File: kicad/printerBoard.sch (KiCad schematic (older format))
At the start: 10 parts

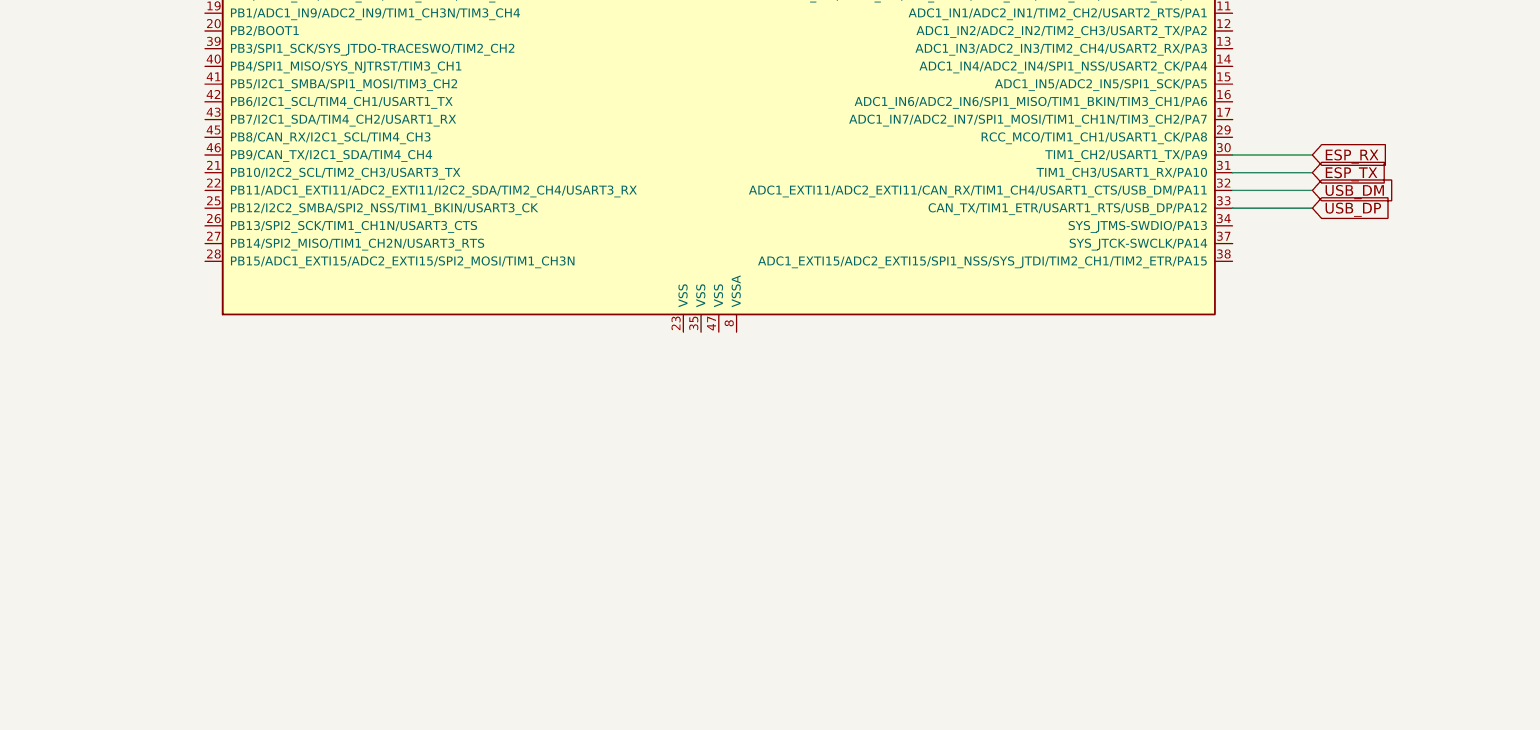
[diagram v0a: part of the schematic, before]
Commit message: Adding A and B motor drivers
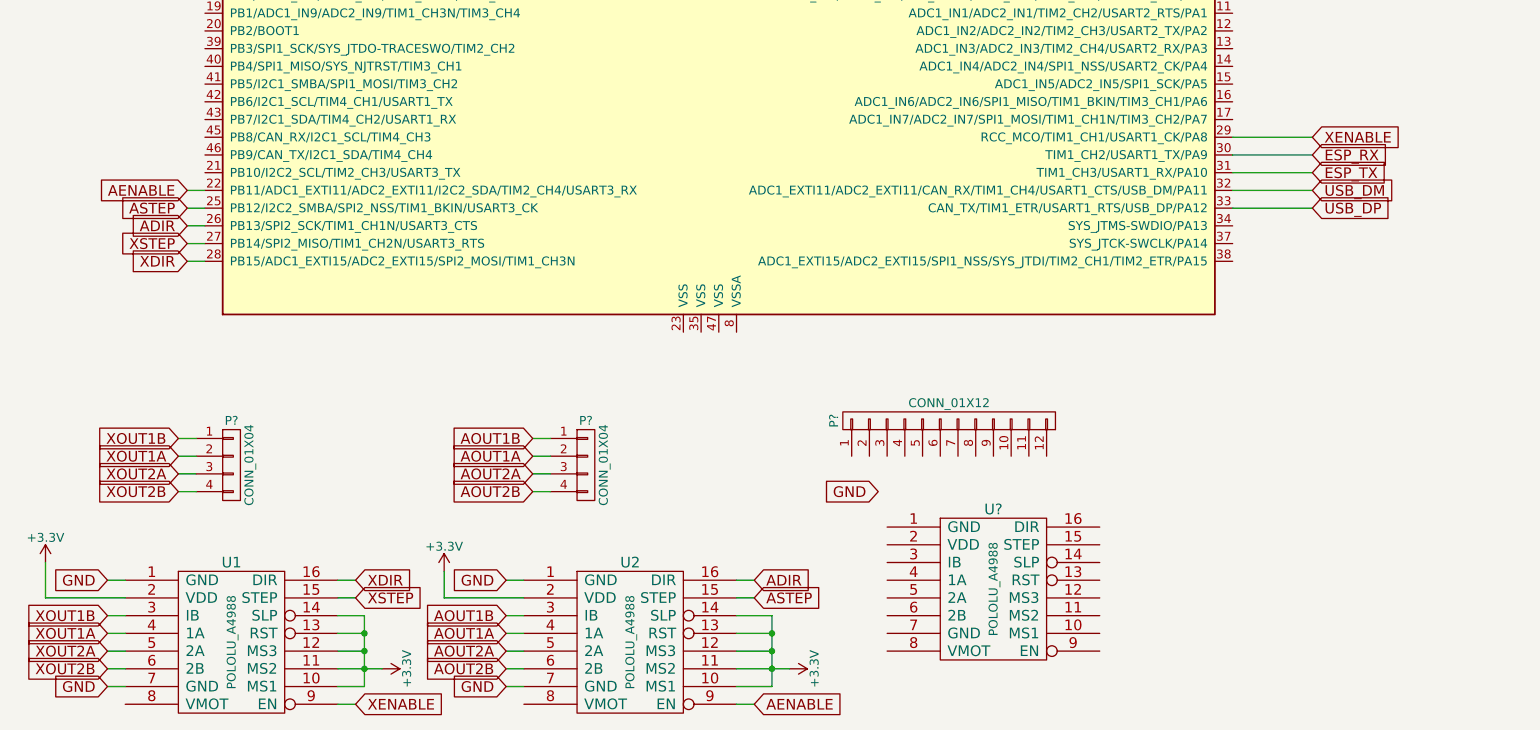
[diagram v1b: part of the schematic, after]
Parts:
- added P? (x2): CONN_01X04, symbol CONN_01X04
- added P?: CONN_01X12, symbol CONN_01X12
- added U1, U2, U?: POLOLU_A4988, symbol POLOLU_A4988
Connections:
- net +3V3: now also U1.10 (MS1), U1.11 (MS2), U1.12 (MS3), U1.13 (RST), U1.14 (SLP), U1.2 (VDD), U2.10 (MS1), U2.11 (MS2), U2.12 (MS3), U2.13 (RST), U2.14 (SLP), U2.2 (VDD)
- net GND: now also U1.1 (GND), U1.7 (GND), U2.1 (GND), U2.7 (GND)
- net AENABLE: now reaches U?.22 (PB11/ADC1_EXTI11/ADC2_EXTI11/I2C2_SDA/TIM2_CH4/USART3_RX)
- net AENABLE: now also U2.9 (EN)
- net ASTEP: now reaches U?.25 (PB12/I2C2_SMBA/SPI2_NSS/TIM1_BKIN/USART3_CK)
- net ASTEP: now also U2.15 (STEP)
- net ADIR: now reaches U?.26 (PB13/SPI2_SCK/TIM1_CH1N/USART3_CTS)
- net ADIR: now also U2.16 (DIR)
- net XSTEP: now reaches U?.27 (PB14/SPI2_MISO/TIM1_CH2N/USART3_RTS)
- net XSTEP: now also U1.15 (STEP)
- net XDIR: now reaches U?.28 (PB15/ADC1_EXTI15/ADC2_EXTI15/SPI2_MOSI/TIM1_CH3N)
- net XDIR: now also U1.16 (DIR)
- net XENABLE: now reaches U?.29 (RCC_MCO/TIM1_CH1/USART1_CK/PA8)
- net XENABLE: now also U1.9 (EN)
- new net AOUT1A: P?.2 (P2), U2.4 (1A)
- new net AOUT1B: P?.1 (P1), U2.3 (IB)
- new net AOUT2A: P?.3 (P3), U2.5 (2A)
- new net AOUT2B: P?.4 (P4), U2.6 (2B)
- new net XOUT1A: P?.2 (P2), U1.4 (1A)
- new net XOUT1B: P?.1 (P1), U1.3 (IB)
- new net XOUT2A: P?.3 (P3), U1.5 (2A)
- new net XOUT2B: P?.4 (P4), U1.6 (2B)

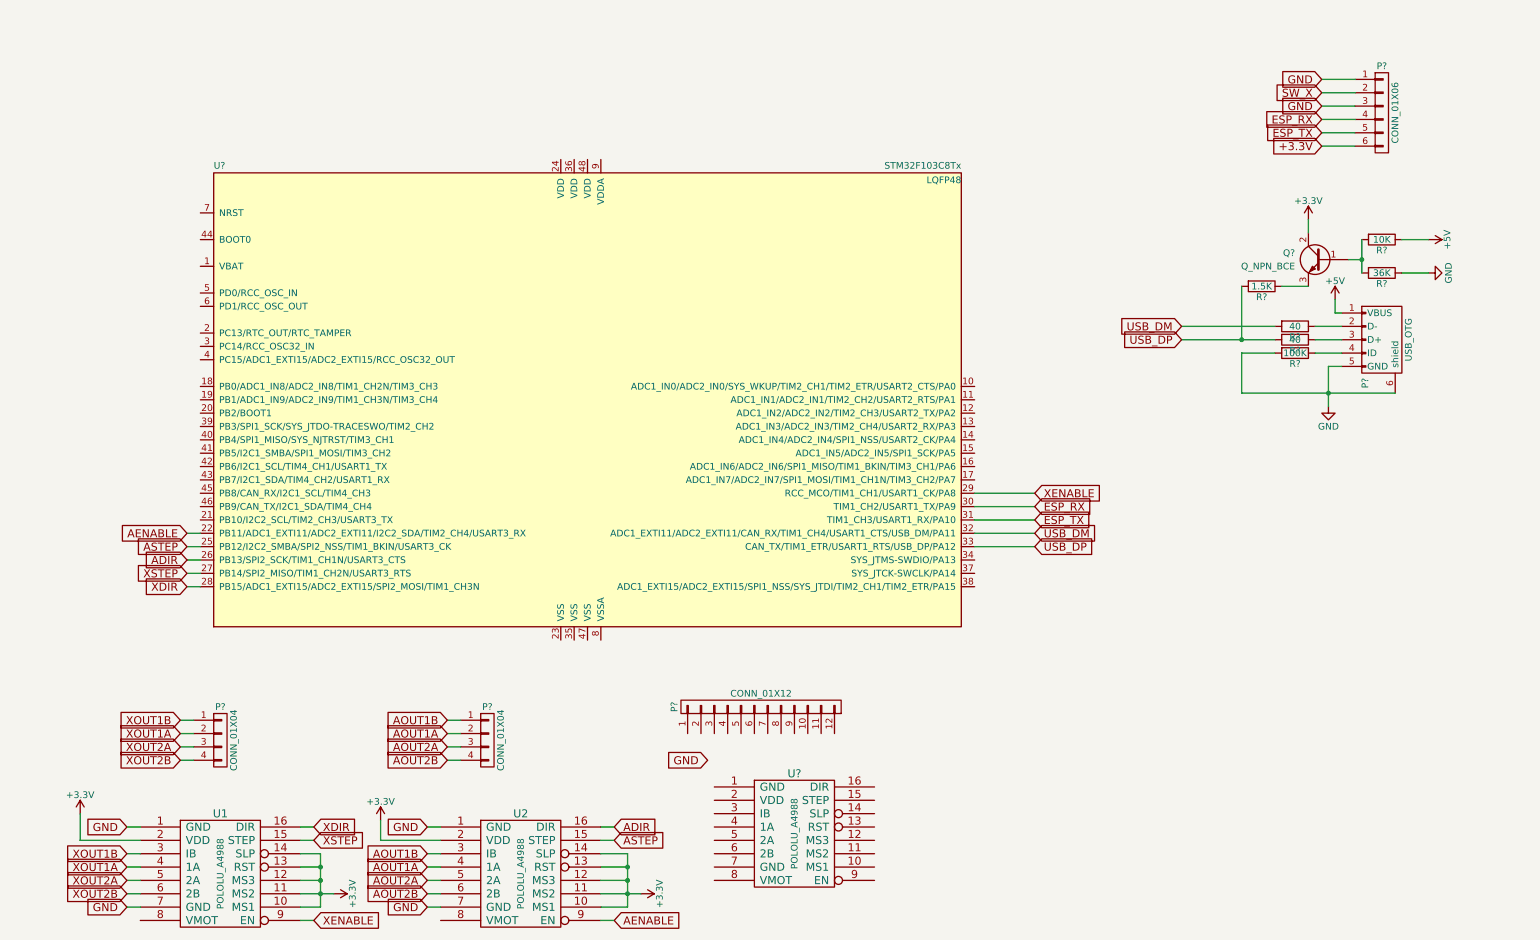
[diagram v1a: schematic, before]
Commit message: Adding mini SD card
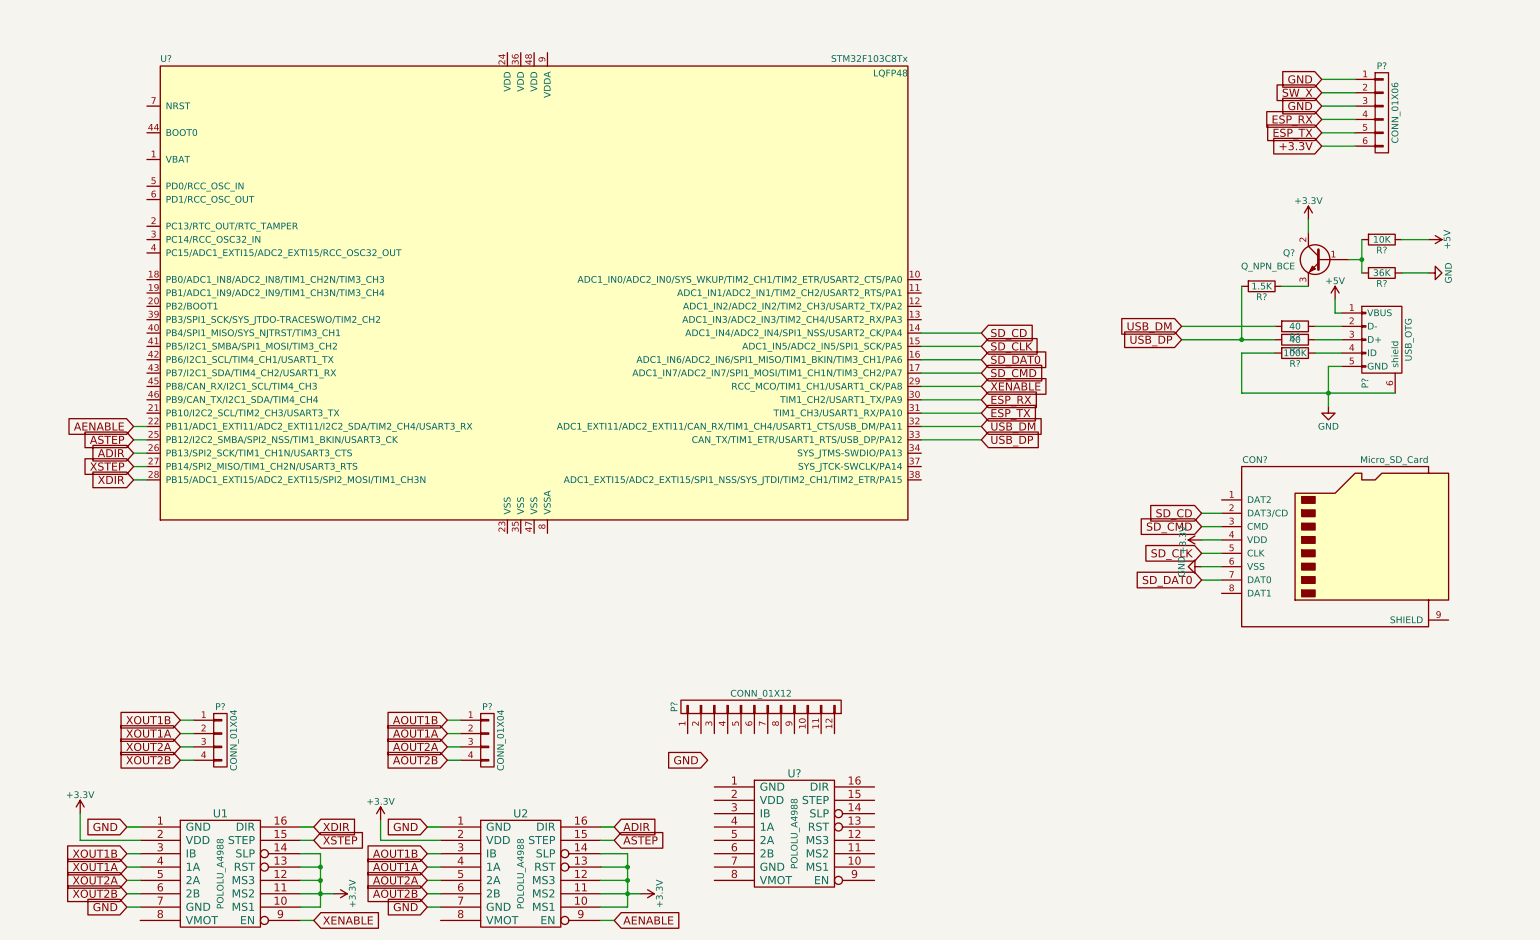
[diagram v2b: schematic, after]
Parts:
- added CON?: Micro_SD_Card, symbol Micro_SD_Card
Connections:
- net +3V3: now also CON?.4 (VDD)
- net GND: now also CON?.6 (VSS)
- net SD_CD: now reaches U?.14 (ADC1_IN4/ADC2_IN4/SPI1_NSS/USART2_CK/PA4)
- net SD_CD: now also CON?.2 (DAT3/CD)
- net SD_CLK: now reaches U?.15 (ADC1_IN5/ADC2_IN5/SPI1_SCK/PA5)
- net SD_CLK: now also CON?.5 (CLK)
- net SD_DAT0: now reaches U?.16 (ADC1_IN6/ADC2_IN6/SPI1_MISO/TIM1_BKIN/TIM3_CH1/PA6)
- net SD_DAT0: now also CON?.7 (DAT0)
- net SD_CMD: now reaches U?.17 (ADC1_IN7/ADC2_IN7/SPI1_MOSI/TIM1_CH1N/TIM3_CH2/PA7)
- net SD_CMD: now also CON?.3 (CMD)
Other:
- moved on the sheet: U?
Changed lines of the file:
@@
 L STM32F103C8Tx U?
 U 1 1 5A4D049D
-P 4500 3600
-F 0 "U?" H 1700 5325 50  0000 L BNN
-F 1 "STM32F103C8Tx" H 7300 5325 50  0000 R BNN
-F 2 "LQFP48" H 7300 5275 50  0000 R TNN
-F 3 "" H 4500 3600 50  0000 C CNN
-	1    4500 3600
+P 4100 2800
+F 0 "U?" H 1300 4525 50  0000 L BNN
+F 1 "STM32F103C8Tx" H 6900 4525 50  0000 R BNN
+F 2 "LQFP48" H 6900 4475 50  0000 R TNN
+F 3 "" H 4100 2800 50  0000 C CNN
+	1    4100 2800
 	1    0    0    -1
 $EndComp
@@
 Wire Wire Line
 	10000 1700 10250 1700
-Text GLabel 7850 4600 2    60   Input ~ 0
+Text GLabel 7450 3800 2    60   Input ~ 0
 USB_DM
-Text GLabel 7850 4700 2    60   Input ~ 0
+Text GLabel 7450 3900 2    60   Input ~ 0
 USB_DP
-Text GLabel 7850 4400 2    60   Input ~ 0
+Text GLabel 7450 3600 2    60   Input ~ 0
 ESP_RX
-Text GLabel 7850 4500 2    60   Input ~ 0
+Text GLabel 7450 3700 2    60   Input ~ 0
 ESP_TX
 Wire Wire Line
-	7400 4400 7850 4400
-Wire Wire Line
-	7400 4500 7850 4500
-Wire Wire Line
-	7400 4600 7850 4600
-Wire Wire Line
-	7850 4700 7400 4700
+	7000 3600 7450 3600
+Wire Wire Line
+	7000 3700 7450 3700
+Wire Wire Line
+	7000 3800 7450 3800
+Wire Wire Line
+	7450 3900 7000 3900
 $Comp
 L POLOLU_A4988 U1
@@
 	0    -1   -1   0
 $EndComp
-Text GLabel 1500 4900 0    60   Input ~ 0
+Text GLabel 1100 4100 0    60   Input ~ 0
 XSTEP
 Text GLabel 2450 6900 2    60   Input ~ 0
@@
 Text GLabel 2450 6800 2    60   Input ~ 0
 XDIR
-Text GLabel 1500 5000 0    60   Input ~ 0
+Text GLabel 1100 4200 0    60   Input ~ 0
 XDIR
 Wire Wire Line
-	1500 4900 1600 4900
-Wire Wire Line
-	1500 5000 1600 5000
+	1100 4100 1200 4100
+Wire Wire Line
+	1100 4200 1200 4200
 Wire Wire Line
 	2450 6800 2350 6800
 Text GLabel 4700 6800 2    60   Input ~ 0
 ADIR
-Text GLabel 1500 4700 0    60   Input ~ 0
+Text GLabel 1100 3900 0    60   Input ~ 0
 ASTEP
-Text GLabel 1500 4800 0    60   Input ~ 0
+Text GLabel 1100 4000 0    60   Input ~ 0
 ADIR
 Wire Wire Line
-	1500 4700 1600 4700
-Wire Wire Line
-	1500 4800 1600 4800
-Text GLabel 7850 4300 2    60   Input ~ 0
+	1100 3900 1200 3900
+Wire Wire Line
+	1100 4000 1200 4000
+Text GLabel 7450 3500 2    60   Input ~ 0
 XENABLE
-Text GLabel 1500 4600 0    60   Input ~ 0
+Text GLabel 1100 3800 0    60   Input ~ 0
 AENABLE
 Wire Wire Line
-	7400 4300 7850 4300
-Wire Wire Line
-	1500 4600 1600 4600
+	7000 3500 7450 3500
+Wire Wire Line
+	1100 3800 1200 3800
 Wire Wire Line
 	2350 7200 2500 7200
@@
 	2350 7000 2500 7000
 Connection ~ 2500 7100
+$Comp
+L Micro_SD_Card CON?
+U 1 1 5A4FD093
+P 10150 4650
+F 0 "CON?" H 9500 5250 50  0000 C CNN
+F 1 "Micro_SD_Card" H 10800 5250 50  0000 R CNN
+F 2 "" H 11300 4950 50  0000 C CNN
+F 3 "" H 10150 4650 50  0000 C CNN
+	1    10150 4650
+	1    0    0    -1
+$EndComp
+$Comp
+L +3.3V #PWR?
+U 1 1 5A4FD75F
+P 9100 4650
+F 0 "#PWR?" H 9100 4500 50  0001 C CNN
+F 1 "+3.3V" H 9100 4790 50  0000 C CNN
+F 2 "" H 9100 4650 50  0000 C CNN
+F 3 "" H 9100 4650 50  0000 C CNN
+	1    9100 4650
+	0    -1   -1   0
+$EndComp
+$Comp
+L GND #PWR?
+U 1 1 5A4FD935
+P 9100 4850
+F 0 "#PWR?" H 9100 4600 50  0001 C CNN
+F 1 "GND" H 9100 4700 50  0000 C CNN
+F 2 "" H 9100 4850 50  0000 C CNN
+F 3 "" H 9100 4850 50  0000 C CNN
+	1    9100 4850
+	0    1    1    0
+$EndComp
+Wire Wire Line
+	9100 4650 9250 4650
+Wire Wire Line
+	9100 4850 9250 4850
+Text GLabel 9100 4450 0    60   Input ~ 0
+SD_CD
+Wire Wire Line
+	9100 4450 9250 4450
+Text GLabel 7450 3100 2    60   Input ~ 0
+SD_CD
+Wire Wire Line
+	7000 3100 7450 3100
+Text GLabel 9100 4550 0    60   Input ~ 0
+SD_CMD
+Text GLabel 7450 3400 2    60   Input ~ 0
+SD_CMD
+Wire Wire Line
+	7000 3400 7450 3400
+Wire Wire Line
+	9100 4550 9250 4550
+Text GLabel 9100 4750 0    60   Input ~ 0
+SD_CLK
+Wire Wire Line
+	9100 4750 9250 4750
+Text GLabel 9100 4950 0    60   Input ~ 0
+SD_DAT0
+Text GLabel 7450 3300 2    60   Input ~ 0
+SD_DAT0
+Wire Wire Line
+	7000 3300 7450 3300
+Text GLabel 7450 3200 2    60   Input ~ 0
+SD_CLK
+Wire Wire Line
+	7000 3200 7450 3200
+Wire Wire Line
+	9100 4950 9250 4950
 $EndSCHEMATC

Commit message: Adding ULN
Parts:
- removed P?: CONN_01X12, symbol CONN_01X12
- added P?: CONN_01X16, symbol CONN_01X16
- added U?: ULN2003A, symbol ULN2003A
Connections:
- net GND: now also U?.8 (GND)
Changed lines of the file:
@@
 Wire Wire Line
 	3300 7400 3400 7400
-$Comp
-L CONN_01X12 P?
-U 1 1 5A4F21C8
-P 5800 5900
-F 0 "P?" H 5800 6550 50  0000 C CNN
-F 1 "CONN_01X12" V 5900 5900 50  0000 C CNN
-F 2 "" H 5800 5900 50  0000 C CNN
-F 3 "" H 5800 5900 50  0000 C CNN
-	1    5800 5900
-	0    -1   -1   0
-$EndComp
 Text GLabel 1100 4100 0    60   Input ~ 0
 XSTEP
@@
 Wire Wire Line
 	9100 4950 9250 4950
+$Comp
+L ULN2003A U?
+U 1 1 5A4EA245
+P 8350 1400
+F 0 "U?" H 8350 1500 50  0000 C CNN
+F 1 "ULN2003A" H 8350 1300 50  0000 C CNN
+F 2 "" H 8350 1400 50  0000 C CNN
+F 3 "" H 8350 1400 50  0000 C CNN
+	1    8350 1400
+	1    0    0    -1
+$EndComp
+$Comp
+L CONN_01X16 P?
+U 1 1 5A4EABEF
+P 6000 5500
+F 0 "P?" H 6000 6350 50  0000 C CNN
+F 1 "CONN_01X16" V 6100 5500 50  0000 C CNN
+F 2 "" H 6000 5500 50  0000 C CNN
+F 3 "" H 6000 5500 50  0000 C CNN
+	1    6000 5500
+	0    -1   -1   0
+$EndComp
 $EndSCHEMATC

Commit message: Adding some more
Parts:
- added P?: Z, symbol CONN_01X02
- added P?: B, symbol CONN_01X02
- added P?: CONN_01X04, symbol CONN_01X04
- added P?: FAN, symbol CONN_01X02
- added R? (x2): 26, symbol R
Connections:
- net +3V3: now also U?.10 (MS1), U?.11 (MS2), U?.12 (MS3), U?.13 (RST), U?.14 (SLP), U?.2 (VDD)
- net AOUT1A: now also P?.4 (P4)
- net AOUT1B: now also P?.3 (P3)
- net AOUT2A: now also P?.5 (P5)
- net AOUT2B: now also P?.6 (P6)
- net GND: now also P?.13 (P13), P?.15 (P15), U?.1 (GND), U?.7 (GND), P?.1 (P1), P?.2 (P2)
- net Bpin1: now reaches U?.11 (ADC1_IN1/ADC2_IN1/TIM2_CH2/USART2_RTS/PA1)
- net Bpin1: now also P?.1 (P1)
- net YDIR: now reaches U?.20 (PB2/BOOT1)
- net YDIR: now also U?.16 (DIR)
- net YSTEP: now reaches U?.21 (PB10/I2C2_SCL/TIM2_CH3/USART3_TX)
- net YSTEP: now also U?.15 (STEP)
- net Zpin2: now reaches U?.41 (PB5/I2C1_SMBA/SPI1_MOSI/TIM3_CH2)
- net Zpin2: now also P?.2 (P2)
- net at U?.42 (PB6/I2C1_SCL/TIM4_CH1/USART1_TX): now also R?.1
- net at U?.43 (PB7/I2C1_SDA/TIM4_CH2/USART1_RX): now also R?.1
- net YENABLE: now reaches U?.45 (PB8/CAN_RX/I2C1_SCL/TIM4_CH3)
- net YENABLE: now also U?.9 (EN)
- net +12V: now reaches U1.8 (VMOT)
- net +12V: now also P?.1 (P1), P?.7 (P7), P?.8 (P8), P?.9 (P9), U2.8 (VMOT), U?.8 (VMOT), P?.1 (P1)
- net YOUT1B: now reaches U?.3 (IB)
- net YOUT1A: now reaches U?.4 (1A)
- net YOUT2A: now reaches U?.5 (2A)
- net YOUT2B: now reaches U?.6 (2B)
- net ULN11: now reaches U?.11 (O6)
- net ULN11: now also P?.2 (P2)
- net ULN12: now reaches U?.12 (O5)
- net ULN12: now also P?.2 (P2)
- net Q1pin2: now reaches P?.10 (P10)
- net Q1pin2: now also P?.11 (P11), P?.12 (P12)
- new net Q1pin1: R?.2
- new net Q5pin1: R?.2

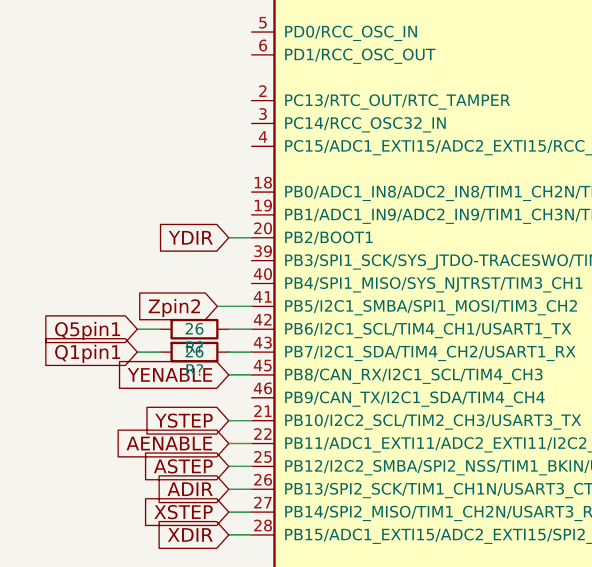
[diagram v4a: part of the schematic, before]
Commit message: adding X-Switch
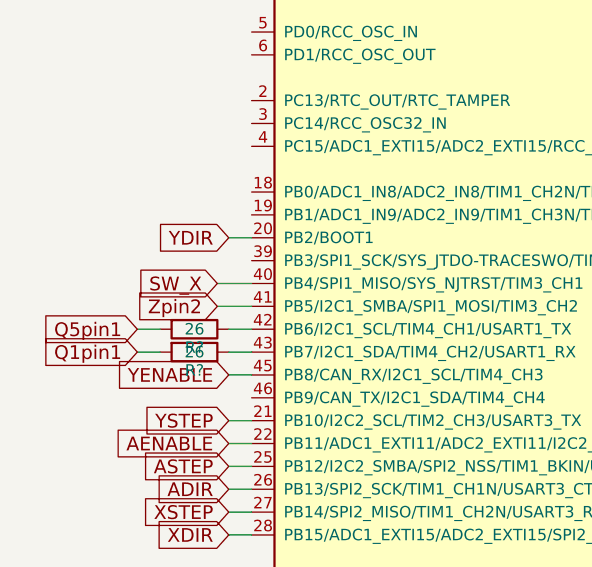
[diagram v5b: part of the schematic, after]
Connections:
- net SW_X: now also U?.40 (PB4/SPI1_MISO/SYS_NJTRST/TIM3_CH1)
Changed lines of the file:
@@
 Wire Wire Line
 	2900 5050 3050 5050
+Text GLabel 1050 3100 0    60   Input ~ 0
+SW_X
+Wire Wire Line
+	1050 3100 1200 3100
 $EndSCHEMATC
